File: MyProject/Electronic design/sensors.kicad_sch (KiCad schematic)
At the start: 5 parts

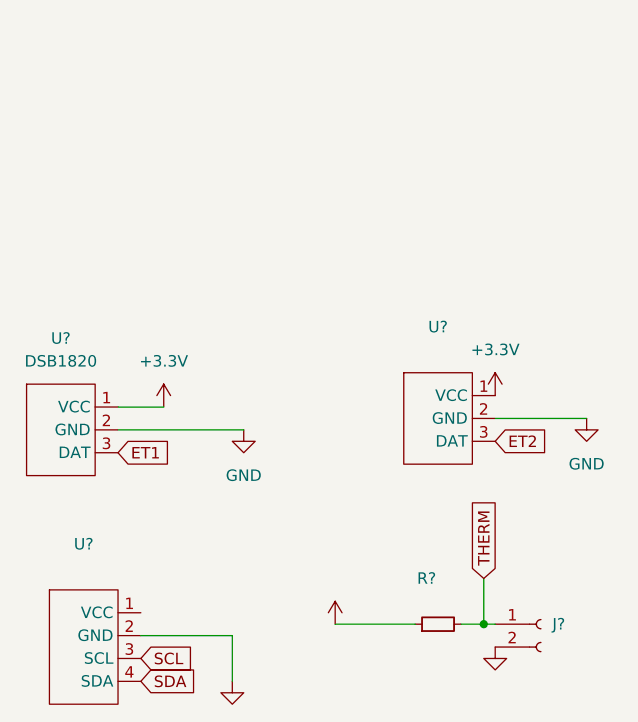
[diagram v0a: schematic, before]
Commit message: Shortening file names for Windows users
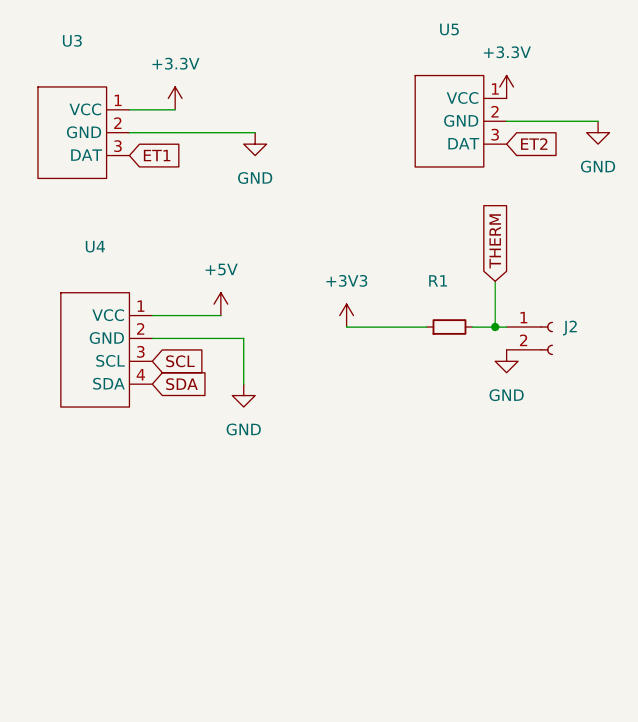
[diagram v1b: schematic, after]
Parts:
- U3: renamed from U?; value DSB1820 -> (none)
- U5: renamed from U?; value ~ -> (none)
- gave numbers to parts that had none: 3
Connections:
- net +5V: now reaches U4.1 (VCC)
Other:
- moved on the sheet: J2, R1, U3, U4, U5
